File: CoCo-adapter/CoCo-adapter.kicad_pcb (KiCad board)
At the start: 2 copper layers, 81.3 x 21.5 mm, 2 parts, among them J5 Bus_ISA_8bit, P1 CoCo-edge

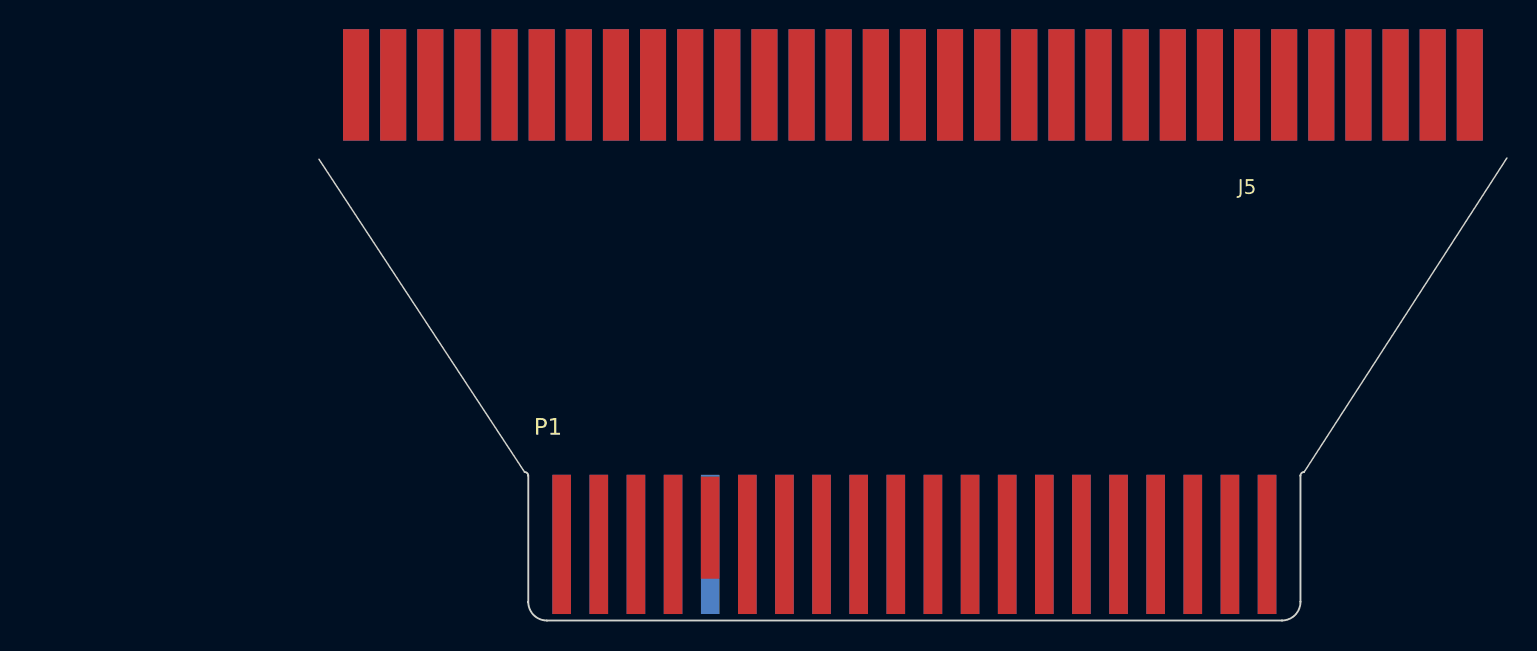
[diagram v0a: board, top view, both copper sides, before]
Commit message: Clean up edge connectors
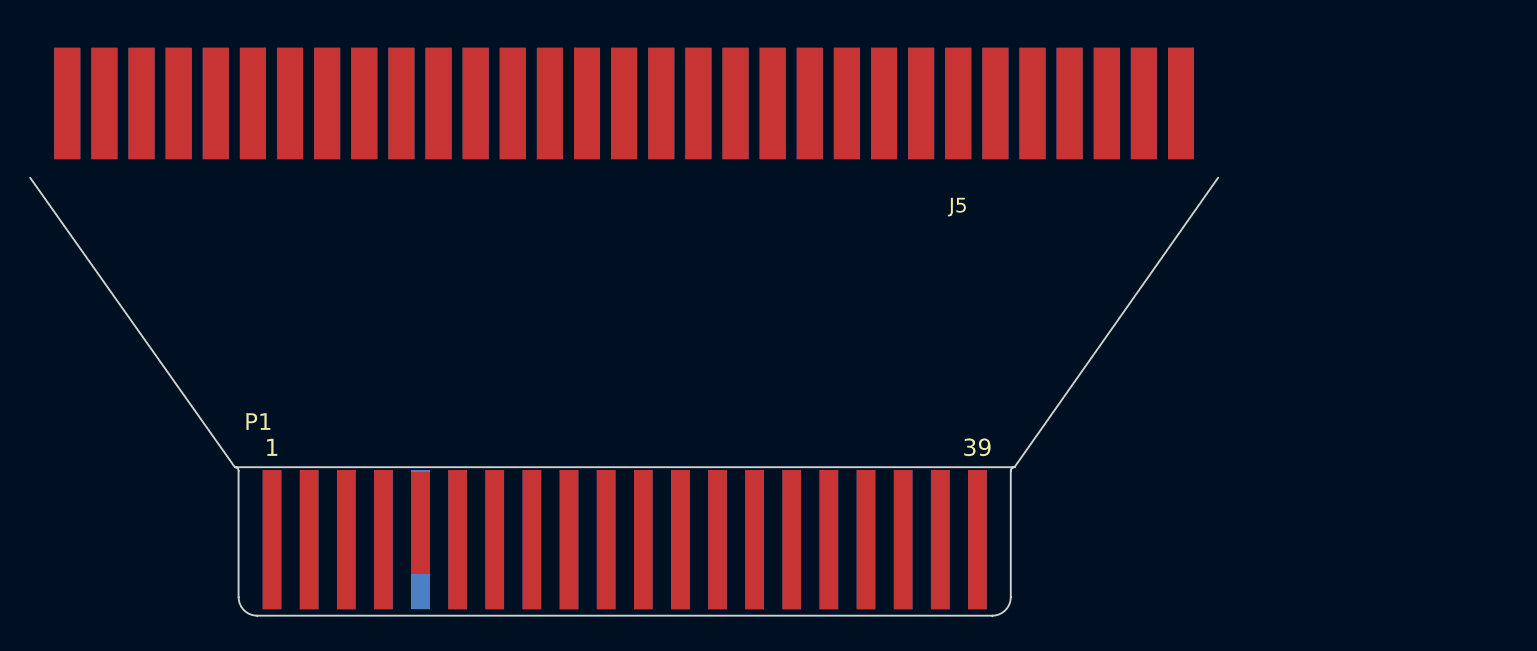
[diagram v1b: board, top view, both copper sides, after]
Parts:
- P1: value CoCo-edge -> COCO-CART
- moved P1 19.8 mm to (74.9, 98.3)
- moved J5 19.8 mm to (63.4, 63.2)
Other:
- board size 81.3 x 21.5 mm -> 81.3 x 19.8 mm

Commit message: Routed CoCo adapter
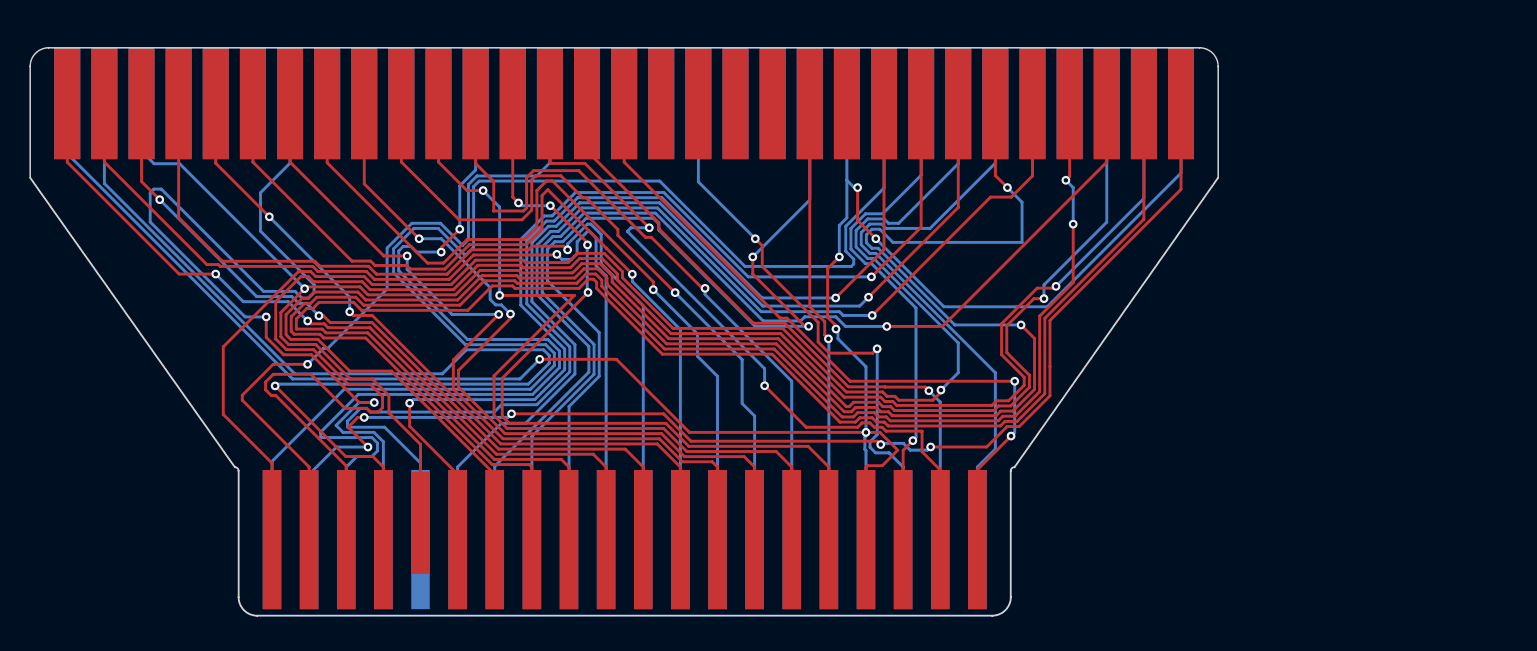
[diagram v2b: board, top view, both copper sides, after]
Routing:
- net /GND: track 0.00 -> 145.2 mm, vias 0 -> 6
- net /D3: track 0.00 -> 122.3 mm, vias 0 -> 2
- net /+5V: track 0.00 -> 120.4 mm, vias 0 -> 2
- net /~{RESET}: track 0.00 -> 117.8 mm, vias 0 -> 1
- net /D7: track 0.00 -> 109.4 mm
- net /D5: track 0.00 -> 105.7 mm, vias 0 -> 2
- net /-12V: track 0.00 -> 99.8 mm, vias 0 -> 1
- net /+12V: track 0.00 -> 95.3 mm
- net /~{NMI}: track 0.00 -> 85.9 mm, vias 0 -> 5
- net /D0: track 0.00 -> 78.5 mm, vias 0 -> 1
- net /Q: track 0.00 -> 76.7 mm, vias 0 -> 1
- net /D6: track 0.00 -> 74.9 mm, vias 0 -> 1
- net /D1: track 0.00 -> 73.4 mm, vias 0 -> 2
- net /D4: track 0.00 -> 71.2 mm, vias 0 -> 1
- net /D2: track 0.00 -> 69.0 mm, vias 0 -> 1
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
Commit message: Add CoCo adapter mounting holes
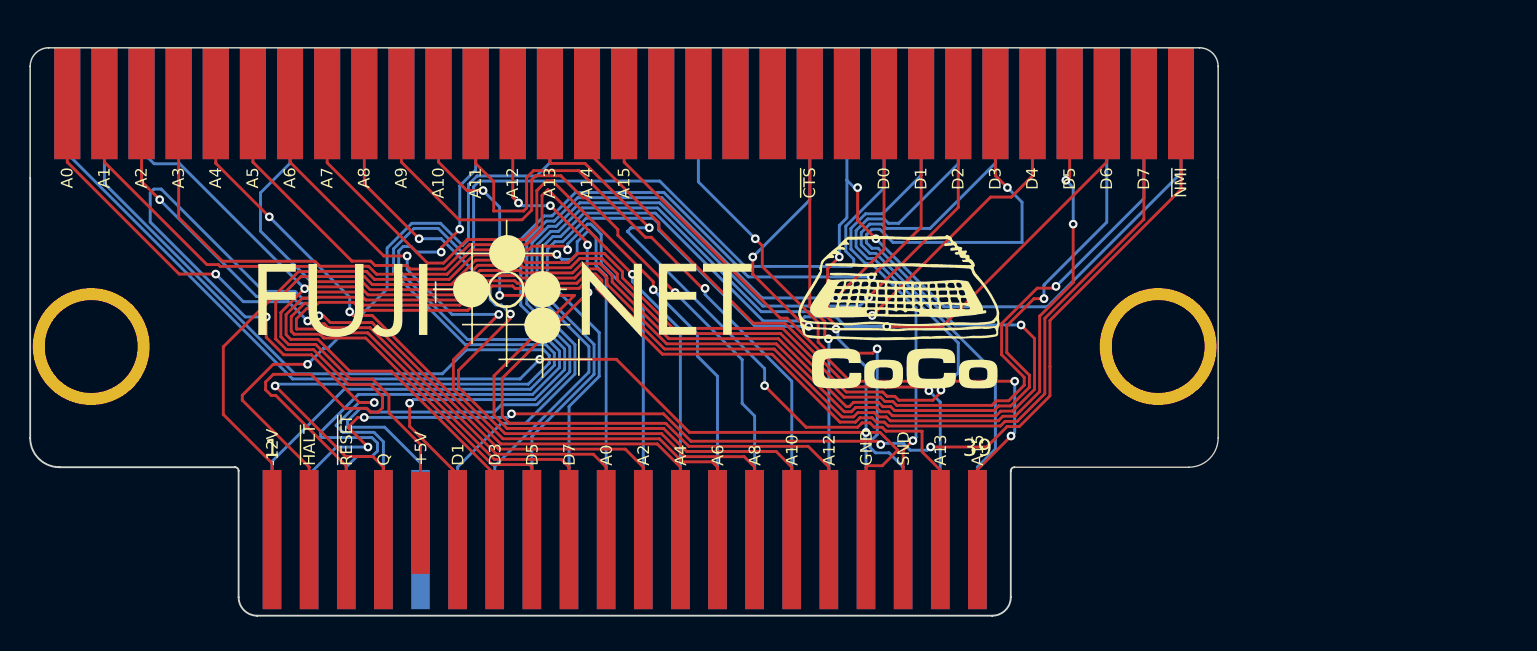
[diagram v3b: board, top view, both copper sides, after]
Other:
- outline, holes or cut-outs redrawn
- board text added: "+12V"
- board text added: "+5V"
- board text added: "-12V"
- board text added: "A0"
- board text added: "A1"
- board text added: "A10"
- board text added: "A11"
- board text added: "A12"
- board text added: "A13"
- board text added: "A14"
- board text added: "A15"
- board text added: "A2"
- board text added: "A3"
- board text added: "A4"
- board text added: "A5"
- board text added: "A6"
- board text added: "A7"
- board text added: "A8"
- board text added: "A9"
- board text added: "D0"
- board text added: "D1"
- board text added: "D2"
- board text added: "D3"
- board text added: "D4"
- board text added: "D5"
- board text added: "D6"
- board text added: "D7"
- board text added: "E"
- board text added: "GND"
- board text added: "Q"
- board text added: "R/~{W}"
- board text added: "SND"
- board text added: "~{CART}"
- board text added: "~{CTS}"
- board text added: "~{HALT}"
- board text added: "~{NMI}"
- board text added: "~{RESET}"
- board text added: "~{SCS}"
- board text added: "~{SLENB}"

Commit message: Add MSX adapter
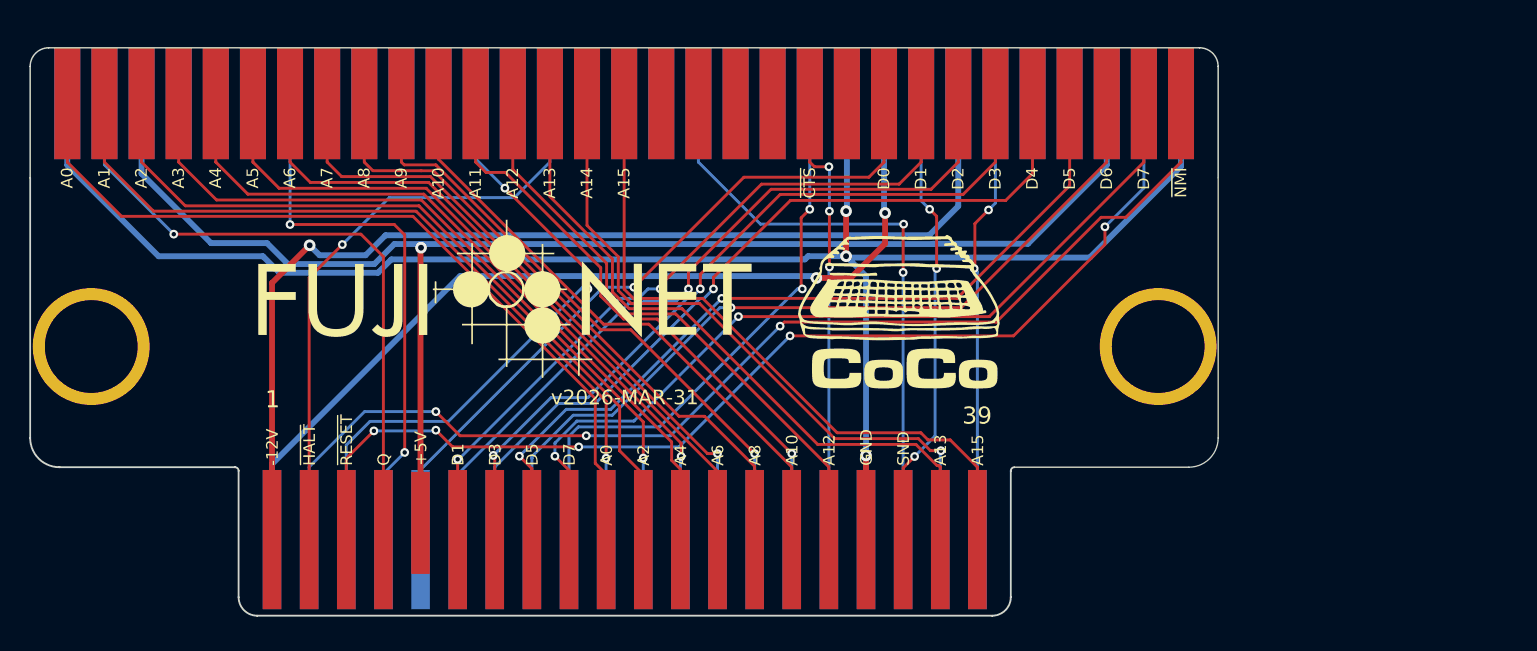
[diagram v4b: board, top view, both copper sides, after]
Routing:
- net /D3: track 122.3 -> 53.1 mm
- net /D7: track 109.4 -> 59.3 mm, vias 0 -> 2
- net /D5: track 105.7 -> 57.0 mm
- net /~{RESET}: track 117.8 -> 75.2 mm, vias 1 -> 5
- net /+12V: track 95.3 -> 63.1 mm, vias 0 -> 2
- net /Q: track 76.7 -> 45.2 mm
- net /D0: track 78.5 -> 49.2 mm
- net /~{CART}: track 66.8 -> 37.9 mm
- net /-12V: track 99.8 -> 74.3 mm
- net /D1: track 73.4 -> 49.8 mm
- net /R/~{W}: track 62.8 -> 40.2 mm
- net /+5V: track 120.4 -> 99.7 mm, vias 2 -> 1
- net /GND: track 145.2 -> 127.0 mm, vias 6 -> 3
- net /D6: track 74.9 -> 57.4 mm
- net /E: track 60.8 -> 44.0 mm
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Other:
- board text added: "v2026-MAR-31"

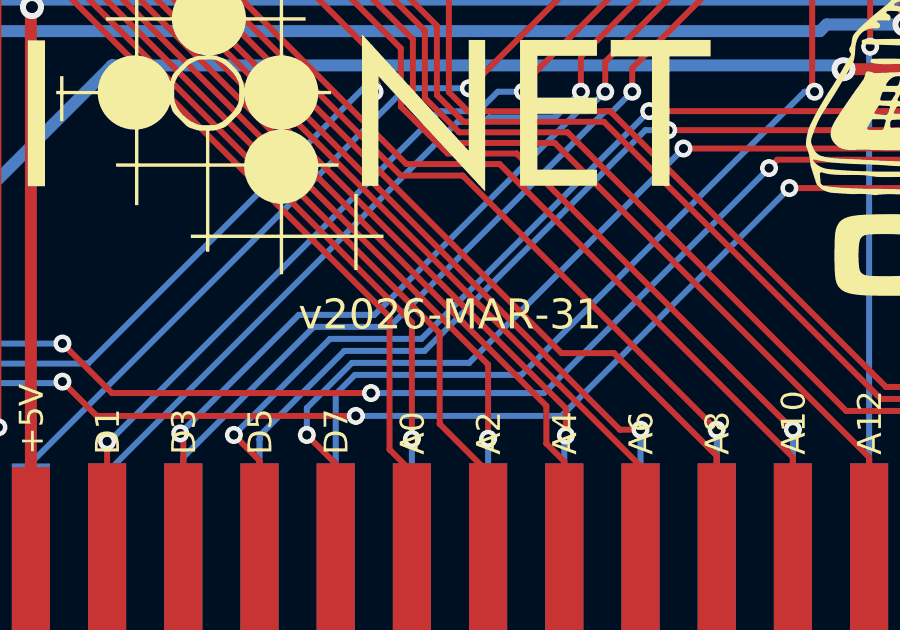
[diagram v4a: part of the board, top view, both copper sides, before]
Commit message: Fix edge cuts and labels
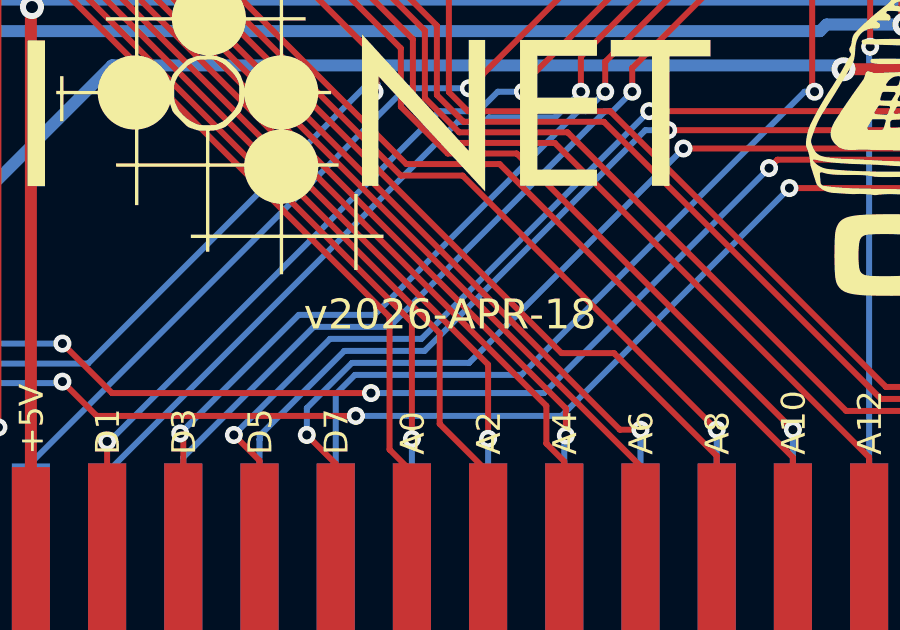
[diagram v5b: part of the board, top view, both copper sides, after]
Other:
- board text added: "v2026-APR-18"
- board text removed: "v2026-MAR-31"
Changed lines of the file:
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@@
 		)
 	)
-	(gr_text "v2026-MAR-31"
+	(gr_text "v2026-APR-18"
 		(at 101.565 83.947 0)
 		(layer "F.SilkS")
@@
 		)
 	)
-	(gr_text "SND"
+	(gr_text "E"
 		(at 83.0072 88.0364 90)
 		(layer "B.SilkS")
